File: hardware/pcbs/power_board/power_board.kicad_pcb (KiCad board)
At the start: 2 copper layers, 90 x 90 mm, 144 parts, among them J1 Header_01x04, J10 Molex 254 47053, J11 Molex 254 47053, J12 Molex 254 47053, J13 Molex 254 47053, J14 Header_02x03, J15 PJ-102AH, J16 ScrewTerminal_02, J17 ScrewTerminal_02, J18 ScrewTerminal_02, J19 ScrewTerminal_02, J2 Header_01x04, J20 ScrewTerminal_02, J21 Header_02x04, J22 ScrewTerminal_02, J3 USB3_B_Micro, J4 USB3_A, J5 USB_A, J6 USB_A, J7 USB_A, J8 USB_A, J9 Molex 254 47053, Q1 BSS138, Q2 BSS138, Q3 BSS138, Q4 BSS138, Q5 IRFR5305, U1 VRB1205S-6WR3, U10 EMC2305, U11 TCA9534, U12 LMR38020, U13 LMR38020, U14 TMP1075D, U2 LTV-247, U3 NCP380, U4 VRB1205S-6WR3, U5 NCP380, U6 VRB1205S-6WR3, U7 NCP380, U8 VRB1205S-6WR3, U9 NCP380

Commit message: power_board: some extra fixes
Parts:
- U12, U13: footprint Package_SO:Texas_R-PDSO-G8_EP2.95x4.9mm_Mask2.4x3.1mm -> ics:Texas_R-PDSO-G8_EP2.95x4.9mm_Mask2.4x3.1mm_ThermalVias
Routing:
- net +12V: track 240.3 -> 240.8 mm
- net GND: vias 144 -> 135
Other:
- board text added: "FOSDEM Power board rev. B"
- board text added: "JLCJLCJLCJLC"

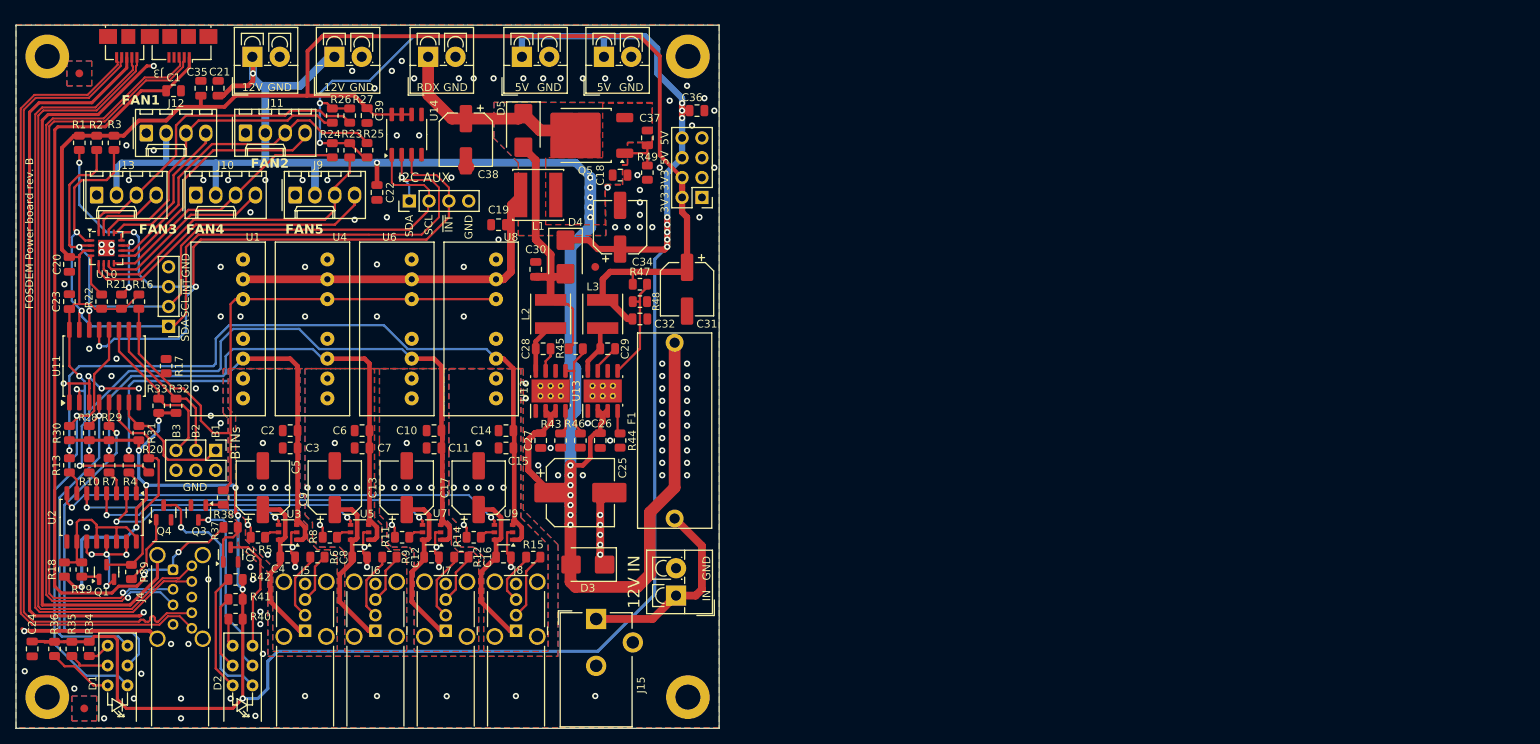
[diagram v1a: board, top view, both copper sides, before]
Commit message: power_board: update components to new versions and annotate
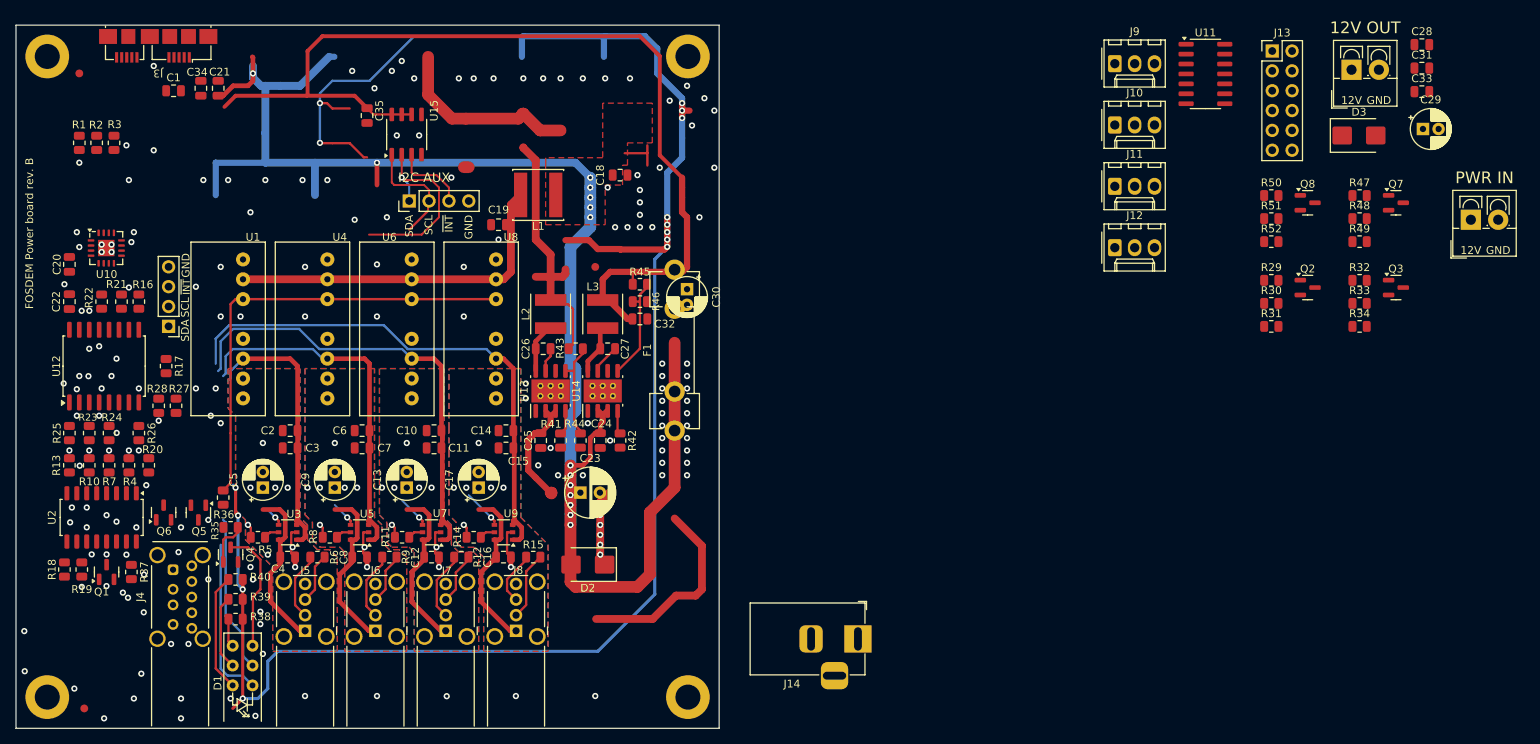
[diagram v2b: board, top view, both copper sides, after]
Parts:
- removed the C22 at (76.2, 105.4)
- removed the C24 at (32.1, 163.8)
- removed the C30 at (96.5, 115.3)
- removed the C34 at (107.3, 109.9)
- removed C36: 100nF, Capacitor_SMD:C_0805_2012Metric
- removed C37: 1μF, Capacitor_SMD:C_0805_2012Metric
- removed C38: 100μF, Capacitor_SMD:CP_Elec_6.3x7.7
- removed the D1 at (43.0, 168.5)
- removed D4, D5: S2A, Diode_SMD:D_SMB
- removed the J14 at (55.6, 138.4)
- removed J17, J18, J19, J20, J22: ScrewTerminal_02, conn:TerminalBlock_4Ucon_1x02_P3.50mm_Vertical
- removed J21: Header_02x04, conn:PinHeader_2x04_P2.54mm_Vertical
- removed the Q5 at (102.9, 98.1)
- removed the R23 at (72.7, 100.0)
- removed the R24 at (70.5, 100.0)
- removed the R25 at (74.9, 100.0)
- removed the R26 at (70.5, 95.6)
- removed the R27 at (72.7, 95.6)
- removed the R35 at (37.1, 163.8)
- removed the R36 at (34.9, 163.8)
- added C28: 1μF, Capacitor_SMD:C_0805_2012Metric, F.Cu at (209.9, 86.5)
- added C29: 100μF, Capacitor_THT:CP_Radial_D5.0mm_P2.00mm, F.Cu at (210.1, 97.3)
- added C31: 1μF, Capacitor_SMD:C_0805_2012Metric, F.Cu at (209.9, 89.5)
- added C33: 100nF, Capacitor_SMD:C_0805_2012Metric, F.Cu at (209.9, 92.5)
- added D3: Zener 15V, Diode_SMD:D_SMB, F.Cu at (201.9, 98.1)
- added J15: ScrewTerminal_02, conn:TerminalBlock_4Ucon_1x02_P3.50mm_Vertical, F.Cu at (216.2, 108.9)
- added Q2: IRML6401, Package_TO_SOT_SMD:SOT-23, F.Cu at (195.3, 117.6)
- added Q3: IRML6401, Package_TO_SOT_SMD:SOT-23, F.Cu at (206.6, 117.6)
- added Q7: IRML6401, Package_TO_SOT_SMD:SOT-23, F.Cu at (206.6, 106.7)
- added Q8: IRML6401, Package_TO_SOT_SMD:SOT-23, F.Cu at (195.3, 106.7)
- added R29: 10kΩ, Resistor_SMD:R_0805_2012Metric, F.Cu at (190.7, 116.7)
- added R30: 4.7kΩ, Resistor_SMD:R_0805_2012Metric, F.Cu at (190.7, 119.6)
- added R31: 10Ω, Resistor_SMD:R_0805_2012Metric, F.Cu at (190.7, 122.6)
- added R32: 10kΩ, Resistor_SMD:R_0805_2012Metric, F.Cu at (202.0, 116.7)
- added R33: 4.7kΩ, Resistor_SMD:R_0805_2012Metric, F.Cu at (202.0, 119.6)
- added R47: 10kΩ, Resistor_SMD:R_0805_2012Metric, F.Cu at (202.0, 105.8)
- added R48: 4.7kΩ, Resistor_SMD:R_0805_2012Metric, F.Cu at (202.0, 108.8)
- added R50: 10kΩ, Resistor_SMD:R_0805_2012Metric, F.Cu at (190.7, 105.8)
- added R51: 4.7kΩ, Resistor_SMD:R_0805_2012Metric, F.Cu at (190.7, 108.8)
- added R52: 10Ω, Resistor_SMD:R_0805_2012Metric, F.Cu at (190.7, 111.7)
- added U11: 4069, Package_SO:SO-14_3.9x8.65mm_P1.27mm, F.Cu at (182.2, 90.2)
- C13, C17, C5, C9: footprint Capacitor_SMD:CP_Elec_6.3x5.4 -> Capacitor_THT:CP_Radial_D5.0mm_P2.00mm
- C23: renamed from C25; footprint Capacitor_SMD:CP_Elec_8x10.5 -> Capacitor_THT:CP_Radial_D6.3mm_P2.50mm
- C30: renamed from C31; footprint Capacitor_SMD:CP_Elec_6.3x5.4 -> Capacitor_THT:CP_Radial_D5.0mm_P2.00mm
- F1: footprint conn:Fuseholder_Littelfuse_625_series_5x20mm -> conn:Fuseholder_FS002
- J10, J11, J12, J9: value Molex 254 47053 -> Molex 22-23-2031; footprint conn:Molex_KK-254_47053 -> Connector_Molex:Molex_KK-254_AE-6410-03A_1x03_P2.54mm_Vertical
- J13: value Molex 254 47053 -> Header_02x06; footprint conn:Molex_KK-254_47053 -> Connector_PinHeader_2.54mm:PinHeader_2x06_P2.54mm_Vertical
- J14: renamed from J15; value PJ-102AH -> Barrel Jack; footprint Connector_BarrelJack:BarrelJack_CUI_PJ-102AH_Horizontal -> Connector_BarrelJack:BarrelJack_Horizontal
- R34: value 1.8kΩ -> 10Ω
- R49: value 100kΩ -> 10Ω
- moved R34 167.8 mm to (202.0, 122.6), turned to 0 degrees
- moved J13 151.6 mm to (190.8, 87.3)
- moved J12 124.8 mm to (170.6, 112.5)
- moved J10 118.0 mm to (170.6, 96.8)
- moved J11 111.5 mm to (170.6, 104.6)
- moved J16 109.6 mm to (200.9, 89.7), turned to 0 degrees
- moved J9 106.3 mm to (170.6, 88.9)
- moved R49 91.6 mm to (202.0, 111.7), turned to 0 degrees
- moved J14 33.6 mm to (137.8, 162.6)
- renumbered C23 to C22, C26 to C24, C27 to C25, C28 to C26, C29 to C27, C35 to C34, C39 to C35, D2 to D1, D3 to D2, Q2 to Q4, Q3 to Q5, Q4 to Q6, R28 to R23, R29 to R24, R30 to R25, R31 to R26, R32 to R27, R33 to R28, R37 to R35, R38 to R36, R39 to R37, R40 to R38, R41 to R39, R42 to R40, R43 to R41, R44 to R42, R45 to R43, R46 to R44, R47 to R45, R48 to R46, U11 to U12, U12 to U13, U13 to U14, U14 to U15
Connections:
- net Net-(J10-Pin_3) renamed /Fan Controller/Fan PWM 2/TACH_IN
- net Net-(J11-Pin_3) renamed /Fan Controller/Fan PWM 3/TACH_IN
- net Net-(J12-Pin_3) renamed /Fan Controller/Fan PWM 4/TACH_IN
- net Net-(J9-Pin_3) renamed /Fan Controller/Fan PWM 1/TACH_IN
- C21 pad 1: +12V -> +5V
- F1 pad 1: Net-(J16-Pin_1) -> Net-(J15-Pin_1)
- J10 pad 2: +12V -> /Fan Controller/Fan PWM 2/FAN_VDD
- J11 pad 2: +12V -> /Fan Controller/Fan PWM 3/FAN_VDD
- J12 pad 2: +12V -> /Fan Controller/Fan PWM 4/FAN_VDD
- J13 pad 1: GND -> /GPIOs/GP0
- J13 pad 3: Net-(J13-Pin_3) -> /GPIOs/GP1
- J13 pad 4: Net-(J13-Pin_4) -> +5V
- J14 pad 1: Net-(J16-Pin_1) -> Net-(J15-Pin_1)
- J16 pad 1: Net-(J16-Pin_1) -> +12V
- J9 pad 2: +12V -> /Fan Controller/Fan PWM 1/FAN_VDD
- L2 pad 2: +6V -> +5V
- R23 pad 1: /GPIOs/LED1 -> /GPIOs/GP0
- R24 pad 1: /GPIOs/LED2 -> /GPIOs/GP1
- R25 pad 1: /GPIOs/LED3 -> /GPIOs/GP2
- R26 pad 1: /GPIOs/BTN1 -> /GPIOs/GP3
- R27 pad 1: /GPIOs/BTN2 -> /GPIOs/GP4
- R28 pad 1: /GPIOs/BTN3 -> /GPIOs/GP5
- R34 pad 2: +5V -> Net-(Q3-G)
- R43 pad 2: +6V -> +5V
- R49 pad 1: GND -> Net-(R49-Pad1)
- U10 pad 13: Net-(J12-Pin_4) -> /Fan Controller/Fan PWM 4/PWM
- U10 pad 15: Net-(J13-Pin_4) -> unconnected-(U10-PWM5-Pad15)
- U10 pad 16: Net-(J13-Pin_3) -> unconnected-(U10-TACH5-Pad16)
- U10 pad 5: Net-(J9-Pin_4) -> /Fan Controller/Fan PWM 1/PWM
- U10 pad 7: Net-(J10-Pin_4) -> /Fan Controller/Fan PWM 2/PWM
- U10 pad 9: Net-(J11-Pin_4) -> /Fan Controller/Fan PWM 3/PWM
- U12 pad 10: /GPIOs/BTN2 -> /GPIOs/GP3
- U12 pad 11: /GPIOs/BTN3 -> /GPIOs/GP4
- U12 pad 12: /GPIOs/LED3 -> /GPIOs/GP5
- U12 pad 4: /GPIOs/LED1 -> /GPIOs/GP0
- U12 pad 5: /GPIOs/LED2 -> /GPIOs/GP1
- U12 pad 7: /GPIOs/BTN1 -> /GPIOs/GP2
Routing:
- net GND: track 256.6 -> 11.2 mm
- net /Indicator LEDs/SBC_ON: track 106.9 -> 0.00 mm
- net /USB Passthrough/SSRX+: track 103.9 -> 0.00 mm
- net /USB Passthrough/SSRX-: track 103.9 -> 0.00 mm
- net /USB Passthrough/SSTX-: track 101.6 -> 0.00 mm
- net /USB Passthrough/SSTX+: track 101.6 -> 0.00 mm
- net /USB Passthrough/D+: track 99.4 -> 0.00 mm
- net /USB Passthrough/D-: track 98.1 -> 0.00 mm
- net /Fan Controller/~{ALERT}: track 102.9 -> 9.58 mm
- net +3.3V: track 219.1 -> 127.1 mm
- net /Fan Controller/SDA: track 103.5 -> 25.3 mm
- net /Fan Controller/SCL: track 92.1 -> 14.9 mm
- net +5V: track 347.0 -> 289.1 mm
- net /GPIOs/LED3: track 57.3 -> 0.00 mm, vias 1 -> 0
- net Net-(U9-~{FLAG}): track 58.7 -> 5.17 mm
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- removed copper zone on B.Cu, net GND
- removed copper zone on F.Cu, net GND

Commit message: power_board: initial outline
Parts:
- moved J14 83.5 mm to (217.0, 136.0), turned to -90 degrees
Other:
- board size 90 x 90 mm -> 94 x 90 mm

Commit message: power_board: route the USB connector
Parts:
- C13, C17, C23, C29, C30, C5, C9, J1, J10, J11, J12, J13, J15, J16, J2, J3, J9, U1, U4, U6, U8: moved to B.Cu
- moved J4 366.3 mm to (408.4, 76.8), turned to -90 degrees
- moved J3 358.7 mm to (405.0, 123.3)
- moved D1 349.9 mm to (393.3, 65.0), turned to -90 degrees
- moved J5 330.3 mm to (385.1, 72.4), turned to -90 degrees
- moved H4 318.1 mm to (340.0, 83.0)
- moved J6 313.0 mm to (376.1, 72.4), turned to -90 degrees
- moved J7 295.8 mm to (367.1, 72.4), turned to -90 degrees
- moved H2 290.6 mm to (323.5, 63.0)
- moved H1 285.0 mm to (400.0, 64.0)
- moved J8 278.7 mm to (358.1, 72.4), turned to -90 degrees
- moved H3 259.3 mm to (372.0, 129.0)
- moved F1 229.6 mm to (332.1, 63.4), turned to -90 degrees
- moved J1 196.0 mm to (231.4, 49.5), turned to 0 degrees
- moved U1 178.5 mm to (221.9, 49.9)
- moved C5 173.9 mm to (219.4, 70.2)
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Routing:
- net +5V: track 289.1 -> 0.00 mm, vias 19 -> 0
- net +12V: track 220.6 -> 5.00 mm, vias 14 -> 0
- net GND: track 11.2 -> 140.2 mm, vias 135 -> 1
- net +3.3V: track 127.1 -> 0.00 mm, vias 3 -> 0
- net Net-(U8-VOUT): track 68.2 -> 0.00 mm, vias 1 -> 0
- net Net-(U6-VOUT): track 59.0 -> 0.00 mm, vias 1 -> 0
- net /GPIOs/GPIO6: track 58.5 -> 0.00 mm
- net /USB Passthrough/SSRX+: track 0.00 -> 57.3 mm
- net /USB Passthrough/SSRX-: track 0.00 -> 55.7 mm
- net /USB Passthrough/SSTX+: track 0.00 -> 51.5 mm
- net /USB Passthrough/D+: track 0.00 -> 50.8 mm, vias 1 -> 0
- net /USB Passthrough/SSTX-: track 0.00 -> 50.2 mm
- net (no net): track 50.0 -> 0.00 mm, vias 1 -> 0
- net /USB Passthrough/D-: track 0.00 -> 48.7 mm, vias 1 -> 0
- net /Indicator LEDs/SBC_ON: track 0.00 -> 47.5 mm, vias 2 -> 0
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- removed copper zone on F.Cu, net +12V
- removed copper zone on B.Cu, net /Isolated chargers/Isolated charger 1/GND-CHG
- removed copper zone on F.Cu, net /Isolated chargers/Isolated charger 1/GND-CHG
- removed copper zone on B.Cu, net /Isolated chargers/Isolated charger 2/GND-CHG
- removed copper zone on F.Cu, net /Isolated chargers/Isolated charger 2/GND-CHG
- removed copper zone on B.Cu, net /Isolated chargers/Isolated charger 3/GND-CHG
- removed copper zone on F.Cu, net /Isolated chargers/Isolated charger 3/GND-CHG
- removed copper zone on B.Cu, net /Isolated chargers/Isolated charger 4/GND-CHG
- removed copper zone on F.Cu, net /Isolated chargers/Isolated charger 4/GND-CHG
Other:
- outline, holes or cut-outs redrawn

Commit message: power_board: route some more components, get closer to finalising shape
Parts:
- removed H2: MountingHole_Pad, MountingHole:MountingHole_3.2mm_M3_DIN965_Pad
- C1, C10, C11, C12, C14, C15, C16, C18, C19, C2, C20, C21, C22, C24, C25, C26, C27, C28, C3, C31, C32, C33, C34, C35, C4, C6, C7, C8, D2, D3, L1, L2, L3, Q1, Q2, Q3, Q4, Q5, Q6, Q7, Q8, R1, R10, R11, R12, R13, R14, R15, R16, R17, R18, R19, R2, R20, R21, R22, R23, R24, R25, R26, R27, R28, R29, R3, R30, R31, R32, R33, R34, R35, R36, R37, R38, R39, R4, R40, R41, R42, R43, R44, R45, R46, R47, R48, R49, R5, R50, R51, R52, R6, R7, R8, R9, U10, U11, U12, U13, U14, U15, U2, U3, U5, U7, U9: moved to B.Cu
- C13, C17, C23, C29, C30, C5, C9, J1, J10, J11, J12, J13, J15, J16, J2, J9, U1, U4, U6, U8: moved to F.Cu
- moved FID3 354.0 mm to (392.0, 148.0)
- moved FID2 315.2 mm to (348.0, 147.5)
- moved J15 282.1 mm to (343.9, 77.2), turned to 0 degrees
- moved D2 240.8 mm to (330.5, 73.7), turned to -90 degrees
- moved FID1 240.3 mm to (338.5, 62.0)
- moved C28 194.9 mm to (15.1, 86.5), turned to 180 degrees
- moved C31 194.9 mm to (15.1, 89.5), turned to 180 degrees
- moved C33 194.9 mm to (15.1, 92.5), turned to 180 degrees
- moved Q3 188.2 mm to (18.4, 117.6), turned to 180 degrees
- moved Q7 188.2 mm to (18.4, 106.7), turned to 180 degrees
- moved R32 178.9 mm to (23.0, 116.7), turned to 180 degrees
- moved R33 178.9 mm to (23.0, 119.6), turned to 180 degrees
- moved R34 178.9 mm to (23.0, 122.6), turned to 180 degrees
- moved R47 178.9 mm to (23.0, 105.8), turned to 180 degrees
- moved R48 178.9 mm to (23.0, 108.8), turned to 180 degrees
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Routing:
- net +12V: track 5.00 -> 31.2 mm
- net Net-(J15-Pin_1): track 21.8 -> 28.6 mm
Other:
- board size 94 x 90 mm -> 87 x 90 mm

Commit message: power_board: arrange route charger units
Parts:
- moved R15 244.0 mm to (360.4, 75.2), turned to -90 degrees
- moved R12 243.7 mm to (369.3, 75.2), turned to -90 degrees
- moved R9 243.7 mm to (378.5, 75.2), turned to -90 degrees
- moved R6 243.4 mm to (387.4, 75.2), turned to -90 degrees
- moved C4 236.5 mm to (387.4, 86.0), turned to 0 degrees
- moved C8 235.0 mm to (376.6, 86.0), turned to 0 degrees
- moved C12 233.5 mm to (365.8, 86.0), turned to 0 degrees
- moved U3 233.3 mm to (386.4, 91.8), turned to 90 degrees
- moved J16 233.0 mm to (331.9, 100.2)
- moved C16 231.9 mm to (355.0, 86.0), turned to 0 degrees
- moved C2 231.8 mm to (388.3, 96.2), turned to -90 degrees
- moved U5 231.7 mm to (375.6, 91.8), turned to 90 degrees
- moved C6 230.2 mm to (377.5, 96.2), turned to -90 degrees
- moved U7 230.2 mm to (364.8, 91.8), turned to 90 degrees
- moved C3 230.0 mm to (386.1, 96.2), turned to -90 degrees
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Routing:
- net +12V: track 31.2 -> 82.4 mm
- net Net-(U3-~{FLAG}): track 0.00 -> 42.2 mm, vias 0 -> 2
- net Net-(R4-Pad1): track 0.00 -> 38.9 mm, vias 0 -> 2
- net Net-(U5-~{FLAG}): track 0.00 -> 35.4 mm, vias 0 -> 2
- net Net-(U9-~{FLAG}): track 0.00 -> 32.9 mm, vias 0 -> 2
- net Net-(R13-Pad1): track 0.00 -> 32.3 mm, vias 0 -> 2
- net Net-(R7-Pad1): track 0.00 -> 32.2 mm, vias 0 -> 2
- net Net-(U7-~{FLAG}): track 0.00 -> 29.2 mm, vias 0 -> 2
- net Net-(R10-Pad1): track 0.00 -> 27.6 mm, vias 0 -> 2
- net Net-(J5-VBUS): track 0.00 -> 25.6 mm
- net Net-(J6-VBUS): track 0.00 -> 24.1 mm
- net Net-(J7-VBUS): track 0.00 -> 21.8 mm
- net Net-(J8-VBUS): track 0.00 -> 21.1 mm
- net Net-(U8-VOUT): track 0.00 -> 10.7 mm
- net Net-(U6-VOUT): track 0.00 -> 10.7 mm
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
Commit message: power_board: arrange charger units
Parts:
- added H2: MountingHole_Pad, MountingHole:MountingHole_3.2mm_M3_DIN965_Pad, F.Cu at (524.4, 95.2)
- moved J13 369.5 mm to (445.5, 115.6), turned to 180 degrees
- moved R38 305.1 mm to (457.8, 67.9), turned to 0 degrees
- moved R39 305.1 mm to (457.8, 65.4), turned to 0 degrees
- moved R40 305.1 mm to (457.8, 62.9), turned to 0 degrees
- moved R37 299.2 mm to (465.8, 64.5), turned to 90 degrees
- moved Q6 297.7 mm to (462.3, 64.1), turned to 180 degrees
- moved Q1 297.1 mm to (468.0, 68.6), turned to 180 degrees
- moved R19 296.1 mm to (469.3, 65.4), turned to 180 degrees
- moved R18 294.8 mm to (469.3, 62.9), turned to 180 degrees
- moved Q4 290.9 mm to (448.0, 74.6)
- moved R36 289.3 mm to (450.2, 78.8), turned to 90 degrees
- moved Q5 289.2 mm to (451.8, 74.6), turned to 90 degrees
- moved R35 288.7 mm to (447.8, 78.8), turned to 90 degrees
- moved R20 277.6 mm to (449.6, 82.9), turned to 180 degrees
- moved R27 274.7 mm to (448.0, 106.7), turned to 0 degrees
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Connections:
- J13 pad 1: /GPIOs/GP0 -> /GPIOs/GP2
- J13 pad 3: /GPIOs/GP1 -> /GPIOs/GP3
- J13 pad 5: /GPIOs/GP2 -> /GPIOs/GP4
- J13 pad 7: /GPIOs/GP3 -> /GPIOs/GP1
- J13 pad 9: /GPIOs/GP4 -> /GPIOs/GP0
- R23 pad 1: /GPIOs/GP0 -> /GPIOs/GP2
- R24 pad 1: /GPIOs/GP1 -> /GPIOs/GP3
- R25 pad 1: /GPIOs/GP2 -> /GPIOs/GP4
- R26 pad 1: /GPIOs/GP3 -> /GPIOs/GP1
- R27 pad 1: /GPIOs/GP4 -> /GPIOs/GP0
- U12 pad 12: /GPIOs/GP5 -> /GPIOs/GP1
- U12 pad 4: /GPIOs/GP0 -> /GPIOs/GP5
- U12 pad 5: /GPIOs/GP1 -> /GPIOs/GP0
- U12 pad 6: /GPIOs/GPIO7 -> /GPIOs/GPIO6
- U12 pad 7: /GPIOs/GP2 -> /GPIOs/GPIO7
- U12 pad 9: /GPIOs/GPIO6 -> /GPIOs/GP2
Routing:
- net /GPIOs/GPIO6: track 0.00 -> 59.8 mm
- net /GPIOs/GPIO7: track 0.00 -> 39.2 mm
- net GND: track 140.2 -> 173.6 mm
- net /Isolated chargers/Isolated charger 1/~{OVERCURRENT}: track 0.00 -> 21.7 mm
- net /GPIOs/GP3: track 0.00 -> 20.9 mm, vias 0 -> 1
- net /GPIOs/GP2: track 0.00 -> 20.7 mm, vias 0 -> 1
- net /GPIOs/GP0: track 0.00 -> 18.9 mm, vias 0 -> 1
- net /GPIOs/GP4: track 0.00 -> 18.3 mm, vias 0 -> 1
- net /GPIOs/GP5: track 0.00 -> 16.1 mm
- net /GPIOs/GP1: track 0.00 -> 15.9 mm, vias 0 -> 1
- net +5V: track 0.00 -> 15.5 mm
- net Net-(D1-RK): track 0.00 -> 13.5 mm, vias 0 -> 1
- net +3.3V: track 0.00 -> 11.5 mm
- net /Fan Controller/~{ALERT}: track 0.00 -> 11.2 mm
- net /Fan Controller/SCL: track 0.00 -> 7.78 mm
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- added copper zone on B.Cu, net /Isolated chargers/Isolated charger 1/GND-CHG
- added copper zone on F.Cu, net /Isolated chargers/Isolated charger 1/GND-CHG
- added copper zone on B.Cu, net /Isolated chargers/Isolated charger 2/GND-CHG
- added copper zone on F.Cu, net /Isolated chargers/Isolated charger 2/GND-CHG
- added copper zone on B.Cu, net /Isolated chargers/Isolated charger 3/GND-CHG
- added copper zone on F.Cu, net /Isolated chargers/Isolated charger 3/GND-CHG
- added copper zone on B.Cu, net /Isolated chargers/Isolated charger 4/GND-CHG
- added copper zone on F.Cu, net /Isolated chargers/Isolated charger 4/GND-CHG
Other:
- outline, holes or cut-outs redrawn

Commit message: power_board: holes with larger keepouts
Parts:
- H1, H2, H3, H4: footprint MountingHole:MountingHole_3.2mm_M3_DIN965_Pad -> conn:MountingHole_3.2mm_M3_keepout
- moved Q2 522.3 mm to (548.8, 60.4), turned to 90 degrees
- moved R33 521.5 mm to (541.9, 66.7), turned to 90 degrees
- moved Q8 521.5 mm to (549.8, 69.0)
- moved R48 521.4 mm to (541.9, 57.2), turned to -90 degrees
- moved R31 521.3 mm to (552.0, 61.3), turned to 90 degrees
- moved R52 520.9 mm to (553.6, 69.9), turned to 90 degrees
- moved Q3 520.9 mm to (537.1, 69.6), turned to 90 degrees
- moved Q7 520.8 mm to (537.1, 60.4), turned to 90 degrees
- moved R34 519.9 mm to (540.3, 70.2), turned to 90 degrees
- moved R49 519.7 mm to (540.3, 61.3), turned to 90 degrees
- moved R30 513.5 mm to (544.1, 57.2), turned to -90 degrees
- moved R32 513.3 mm to (534.2, 70.5), turned to 90 degrees
- moved R51 511.5 mm to (544.1, 66.7), turned to 90 degrees
- moved R47 509.9 mm to (531.7, 70.5), turned to 90 degrees
- moved U11 505.3 mm to (547.9, 75.0), turned to -90 degrees
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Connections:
- U11 pad 1: /Fan Controller/Fan PWM 1/PWM -> /Fan Controller/Fan PWM 3/PWM
- U11 pad 2: Net-(R49-Pad1) -> Net-(R34-Pad1)
- U11 pad 3: /Fan Controller/Fan PWM 2/PWM -> /Fan Controller/Fan PWM 1/PWM
- U11 pad 4: Net-(R31-Pad1) -> Net-(R49-Pad1)
- U11 pad 5: /Fan Controller/Fan PWM 3/PWM -> /Fan Controller/Fan PWM 4/PWM
- U11 pad 6: Net-(R34-Pad1) -> Net-(R52-Pad1)
- U11 pad 8: Net-(R52-Pad1) -> Net-(R31-Pad1)
- U11 pad 9: /Fan Controller/Fan PWM 4/PWM -> /Fan Controller/Fan PWM 2/PWM
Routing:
- net Net-(J15-Pin_1): track 29.5 -> 111.6 mm
- net +12V: track 82.4 -> 146.9 mm
- net /Fan Controller/Fan PWM 2/PWM: track 0.00 -> 42.1 mm, vias 0 -> 3
- net /Fan Controller/Fan PWM 1/PWM: track 0.00 -> 39.7 mm, vias 0 -> 2
- net /Fan Controller/Fan PWM 4/TACH_IN: track 0.00 -> 35.2 mm, vias 0 -> 2
- net /Fan Controller/Fan PWM 4/PWM: track 0.00 -> 34.6 mm, vias 0 -> 3
- net /Fan Controller/Fan PWM 3/PWM: track 0.00 -> 33.1 mm, vias 0 -> 3
- net /Fan Controller/Fan PWM 2/TACH_IN: track 0.00 -> 24.6 mm
- net Net-(R31-Pad1): track 0.00 -> 18.6 mm
- net Net-(R49-Pad1): track 0.00 -> 16.7 mm
- net /Fan Controller/Fan PWM 3/TACH_IN: track 0.00 -> 14.2 mm
- net Net-(R34-Pad1): track 0.00 -> 6.03 mm
- net Net-(R52-Pad1): track 0.00 -> 4.26 mm
- net Net-(Q8-G): track 0.00 -> 3.28 mm
- net /Fan Controller/Fan PWM 4/FAN_VDD: track 0.00 -> 3.18 mm
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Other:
- outline, holes or cut-outs redrawn
